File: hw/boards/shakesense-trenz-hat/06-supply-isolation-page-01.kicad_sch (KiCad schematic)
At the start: 12 parts, among them U40 TLV1117LV33DCYR, U41 SN74LVC8T245PWR, U42 SN74LVC8T245PWR

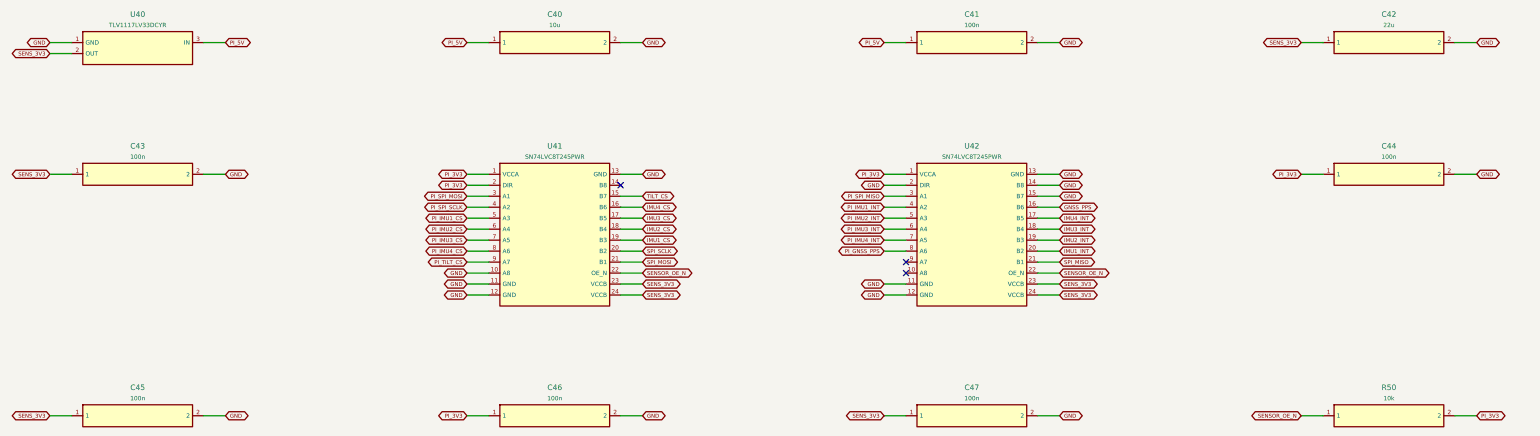
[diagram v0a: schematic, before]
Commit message: Expose Trenz GPIOs on the Pi-outline HDI sensor HAT
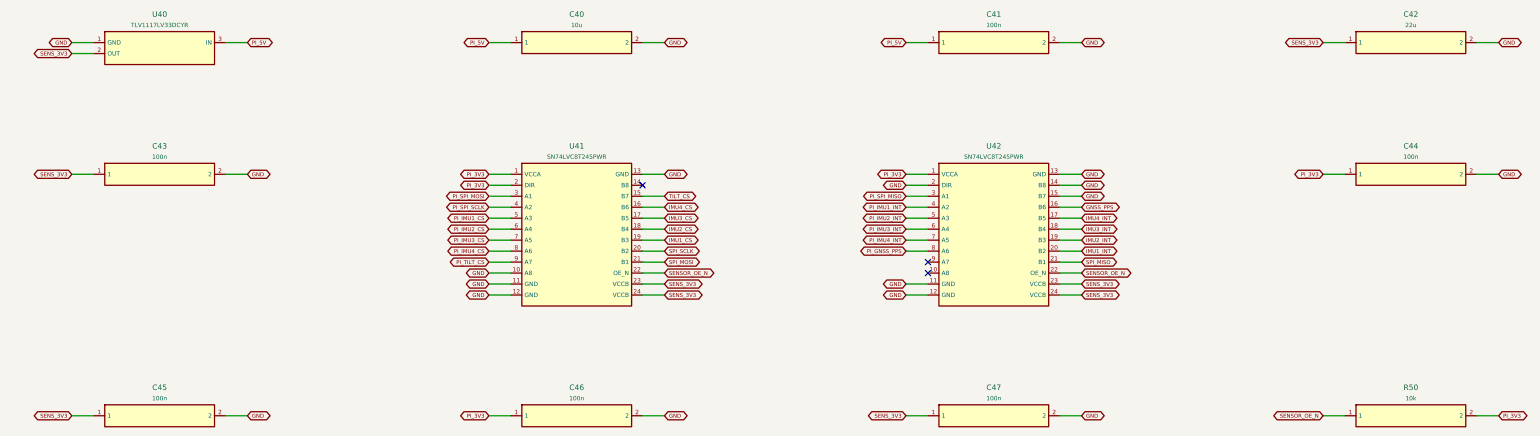
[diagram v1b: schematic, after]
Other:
- title: shakesense-trenz-hat / 06-supply-isolation-page-01 -> ShakeSense T1 / 06-supply-isolation-page-01
- moved on the sheet: C40, C41, C42, C43, C44, C45, C46, C47, R50, U40, U41, U42

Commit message: Replace T1 GNSS with single Racotech geophone input
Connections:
- net GNSS_PPS renamed GEO_DRDY_N
- net PI_GNSS_PPS renamed PI_GEO_DRDY_N
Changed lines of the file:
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@@
-(kicad_sch (version 20230121) (generator eeschema) (paper "A3") (title_block (title "ShakeSense T1 / 06-supply-isolation-page-01") (date "2026-09-24") (rev "T1-GPIO"))
+(kicad_sch (version 20230121) (generator eeschema) (paper "A3") (title_block (title "ShakeSense T1 / 06-supply-isolation-page-01") (date "2026-09-24") (rev "T1-GEO"))
 (symbol (lib_id "ShakeSense:Part_U40") (at 50.8 39.370000000000005 0) (unit 1) (in_bom yes) (on_board yes) (dnp no)
               (property "Reference" "U40" (at 50.8 31.560000000000002 0) (effects (font (size 1.27 1.27))))
@@
 (global_label "PI_IMU4_INT" (shape bidirectional) (at 223.52 83.82 180) (effects (font (size 0.9 0.9)) (justify right)))
 (wire (pts (xy 228.6 86.36) (xy 223.52 86.36)) (stroke (width 0) (type default)))
-(global_label "PI_GNSS_PPS" (shape bidirectional) (at 223.52 86.36 180) (effects (font (size 0.9 0.9)) (justify right)))
+(global_label "PI_GEO_DRDY_N" (shape bidirectional) (at 223.52 86.36 180) (effects (font (size 0.9 0.9)) (justify right)))
 (no_connect (at 228.6 88.9))
 (no_connect (at 228.6 91.44))
@@
 (global_label "GND" (shape bidirectional) (at 264.16 73.66 0) (effects (font (size 0.9 0.9)) (justify left)))
 (wire (pts (xy 259.08 76.2) (xy 264.16 76.2)) (stroke (width 0) (type default)))
-(global_label "GNSS_PPS" (shape bidirectional) (at 264.16 76.2 0) (effects (font (size 0.9 0.9)) (justify left)))
+(global_label "GEO_DRDY_N" (shape bidirectional) (at 264.16 76.2 0) (effects (font (size 0.9 0.9)) (justify left)))
 (wire (pts (xy 259.08 78.74) (xy 264.16 78.74)) (stroke (width 0) (type default)))
 (global_label "IMU4_INT" (shape bidirectional) (at 264.16 78.74 0) (effects (font (size 0.9 0.9)) (justify left)))
